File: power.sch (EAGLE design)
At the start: 27 parts

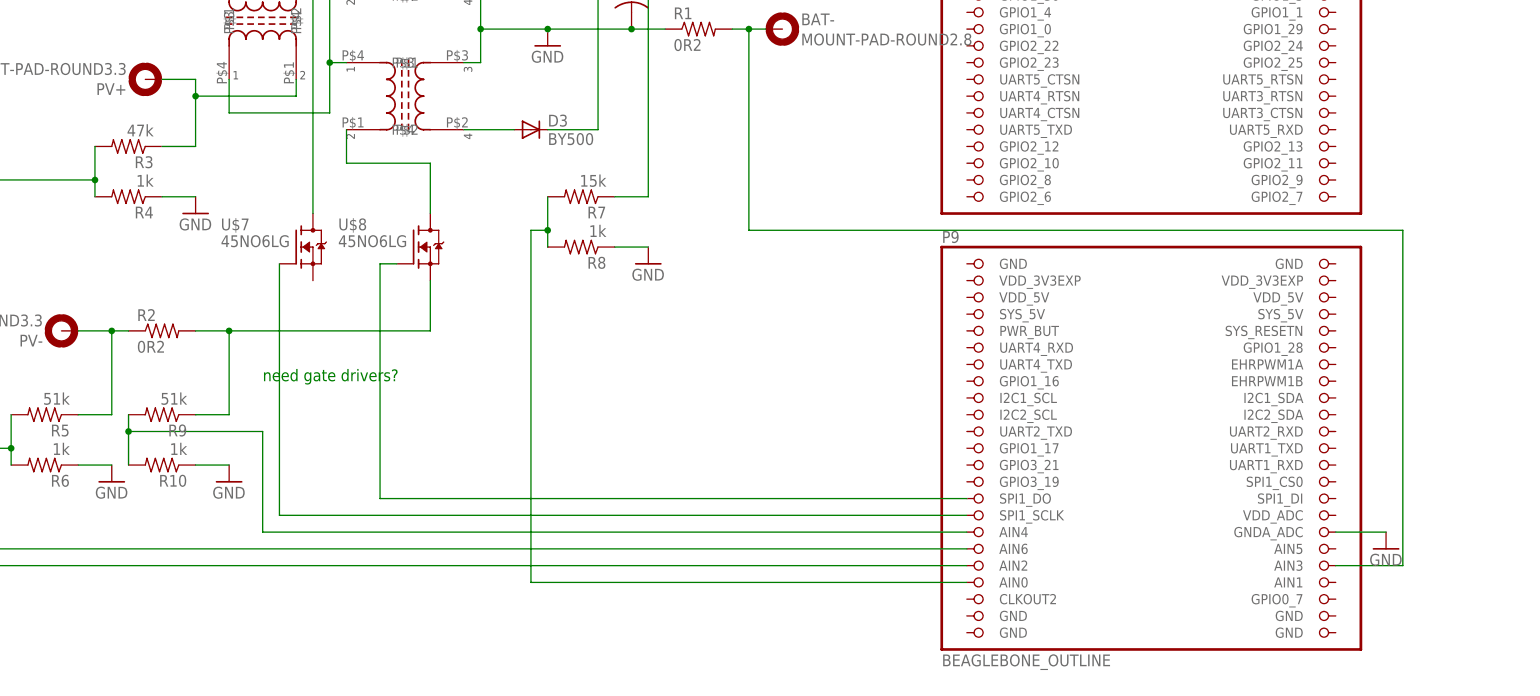
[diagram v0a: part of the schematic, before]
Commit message: more board and schematic fixes.  added slightly negative voltage reference hack.
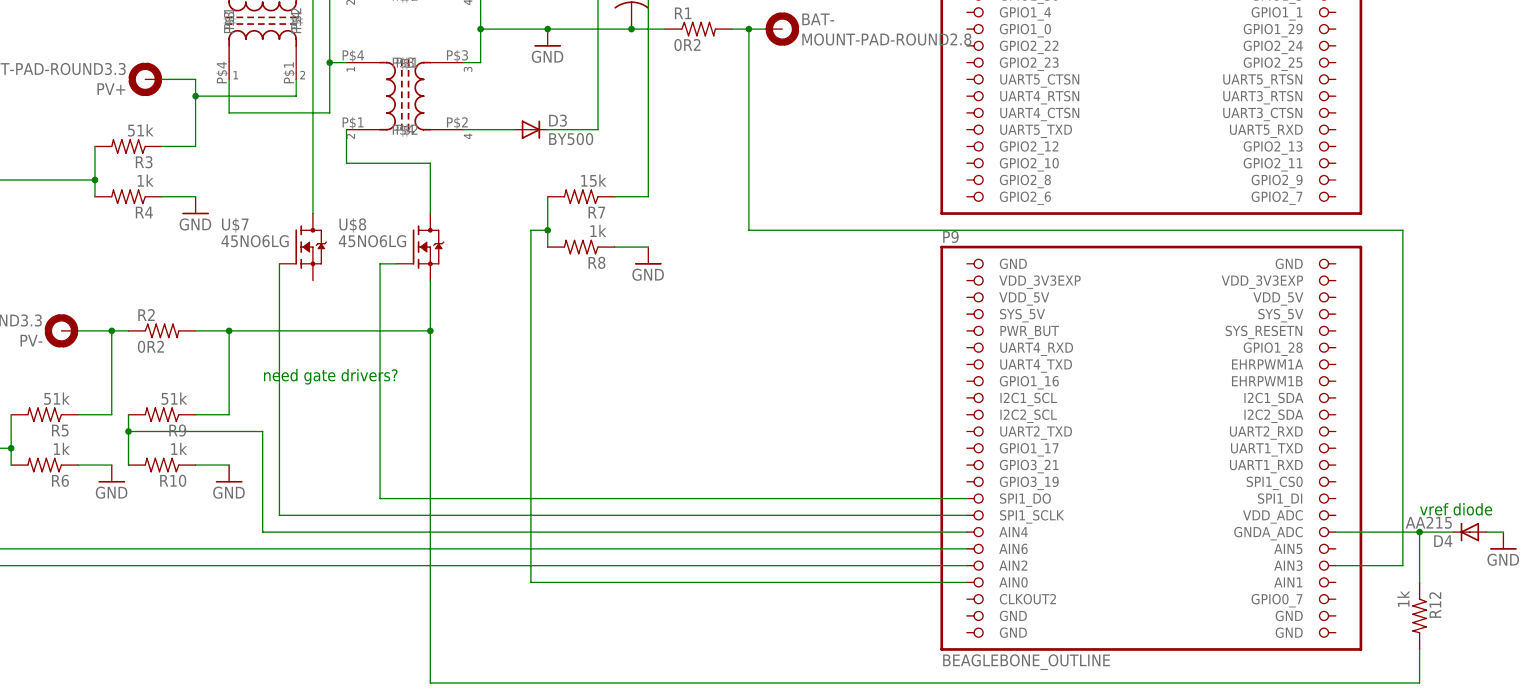
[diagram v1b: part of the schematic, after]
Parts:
- added D4: AA215, diode:AA215
- added R12: 1k, rcl:R-US_R0603
- R3: value 47k -> 51k
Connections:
- new net N$14: D4.C, R12.1, U$6.GNDA_ADC
- net GND: now also D4.A; no longer U$6.GNDA_ADC
- net N$8: now also R12.2
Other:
- note added: "vref diode"
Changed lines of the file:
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@@
 <part name="U$6" library="adafruit" deviceset="BEAGLEBONE_OUTLINE" device=""/>
 <part name="GND1" library="supply1" deviceset="GND" device=""/>
-<part name="R3" library="rcl" deviceset="R-US_" device="R0603" value="47k"/>
+<part name="R3" library="rcl" deviceset="R-US_" device="R0603" value="51k"/>
 <part name="R4" library="rcl" deviceset="R-US_" device="R0603" value="1k"/>
 <part name="GND2" library="supply1" deviceset="GND" device=""/>
@@
 <part name="H3" library="holes" deviceset="MOUNT-PAD-ROUND" device="2.8"/>
 <part name="R7" library="rcl" deviceset="R-US_" device="R0603" value="15k"/>
+<part name="D4" library="diode" deviceset="AA215" device=""/>
+<part name="R12" library="rcl" deviceset="R-US_" device="R0603" value="1k"/>
 <part name="GND7" library="supply1" deviceset="GND" device=""/>
 </parts>
@@
 <plain>
 <text x="17.78" y="-2.54" size="1.778" layer="91">need gate drivers?</text>
+<text x="193.04" y="-22.86" size="1.778" layer="91">vref diode</text>
 </plain>
 <instances>
@@
 <instance part="H3" gate="G$1" x="83.82" y="81.28"/>
 <instance part="R7" gate="G$1" x="66.04" y="25.4" rot="R180"/>
-<instance part="GND7" gate="1" x="187.96" y="-27.94"/>
+<instance part="D4" gate="1" x="200.66" y="-25.4" rot="R180"/>
+<instance part="R12" gate="G$1" x="193.04" y="-38.1" rot="R270"/>
+<instance part="GND7" gate="1" x="205.74" y="-27.94"/>
 </instances>
 <busses>
@@
 </segment>
 <segment>
-<pinref part="GND7" gate="1" pin="GND"/>
-<pinref part="U$6" gate="G$1" pin="GNDA_ADC"/>
-<wire x1="180.34" y1="-25.4" x2="187.96" y2="-25.4" width="0.1524" layer="91"/>
-</segment>
-<segment>
 <pinref part="R8" gate="G$1" pin="1"/>
 <wire x1="71.12" y1="17.78" x2="76.2" y2="17.78" width="0.1524" layer="91"/>
@@
 <wire x1="78.74" y1="81.28" x2="78.74" y2="76.2" width="0.1524" layer="91"/>
 <junction x="78.74" y="76.2"/>
+</segment>
+<segment>
+<pinref part="GND7" gate="1" pin="GND"/>
+<pinref part="D4" gate="1" pin="A"/>
+<wire x1="205.74" y1="-25.4" x2="203.2" y2="-25.4" width="0.1524" layer="91"/>
 </segment>
 </net>
@@
 <pinref part="U$8" gate="G$1" pin="S"/>
 <wire x1="43.18" y1="12.7" x2="43.18" y2="5.08" width="0.1524" layer="91"/>
+<wire x1="43.18" y1="5.08" x2="43.18" y2="-48.26" width="0.1524" layer="91"/>
+<wire x1="43.18" y1="-48.26" x2="193.04" y2="-48.26" width="0.1524" layer="91"/>
+<junction x="43.18" y="5.08"/>
+<pinref part="R12" gate="G$1" pin="2"/>
+<wire x1="193.04" y1="-43.18" x2="193.04" y2="-48.26" width="0.1524" layer="91"/>
 </segment>
 </net>
@@
 </segment>
 </net>
+<net name="N$14" class="0">
+<segment>
+<pinref part="U$6" gate="G$1" pin="GNDA_ADC"/>
+<wire x1="180.34" y1="-25.4" x2="193.04" y2="-25.4" width="0.1524" layer="91"/>
+<pinref part="D4" gate="1" pin="C"/>
+<pinref part="R12" gate="G$1" pin="1"/>
+<wire x1="193.04" y1="-25.4" x2="198.12" y2="-25.4" width="0.1524" layer="91"/>
+<wire x1="193.04" y1="-33.02" x2="193.04" y2="-25.4" width="0.1524" layer="91"/>
+<junction x="193.04" y="-25.4"/>
+</segment>
+</net>

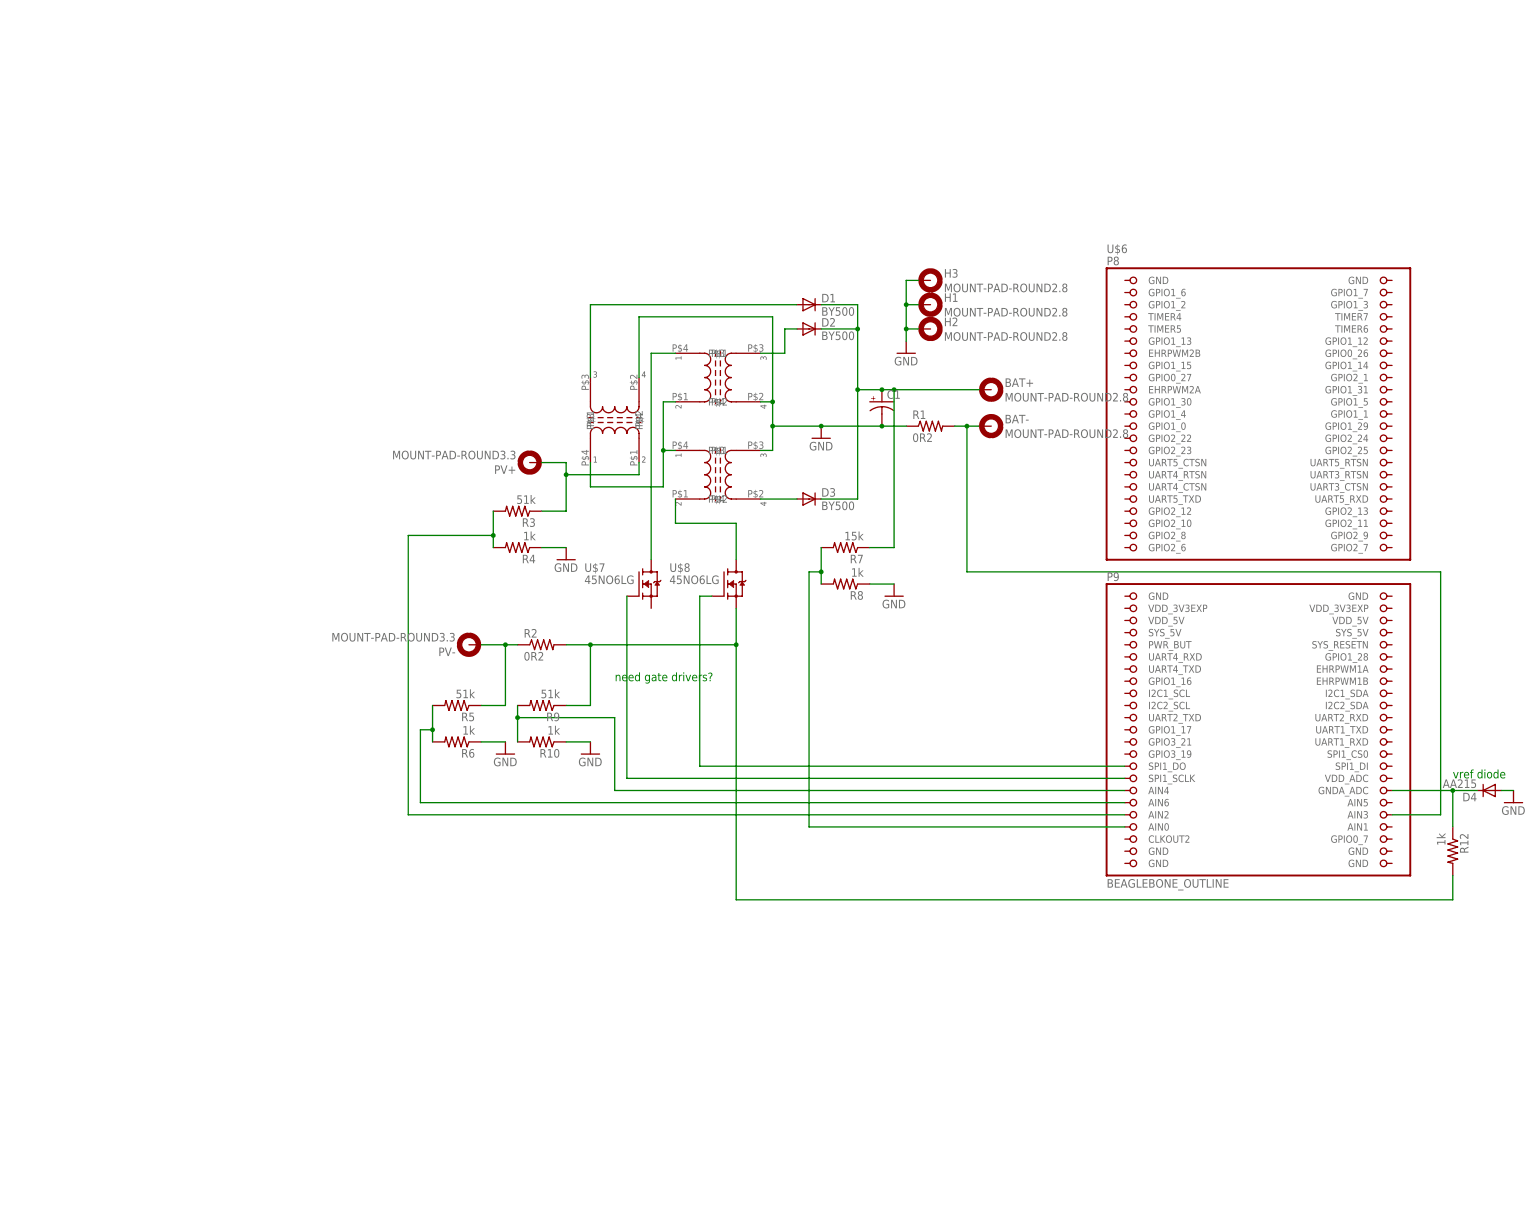
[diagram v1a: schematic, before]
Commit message: made things more complicated, fixed a schematic mistake, added gate drivers
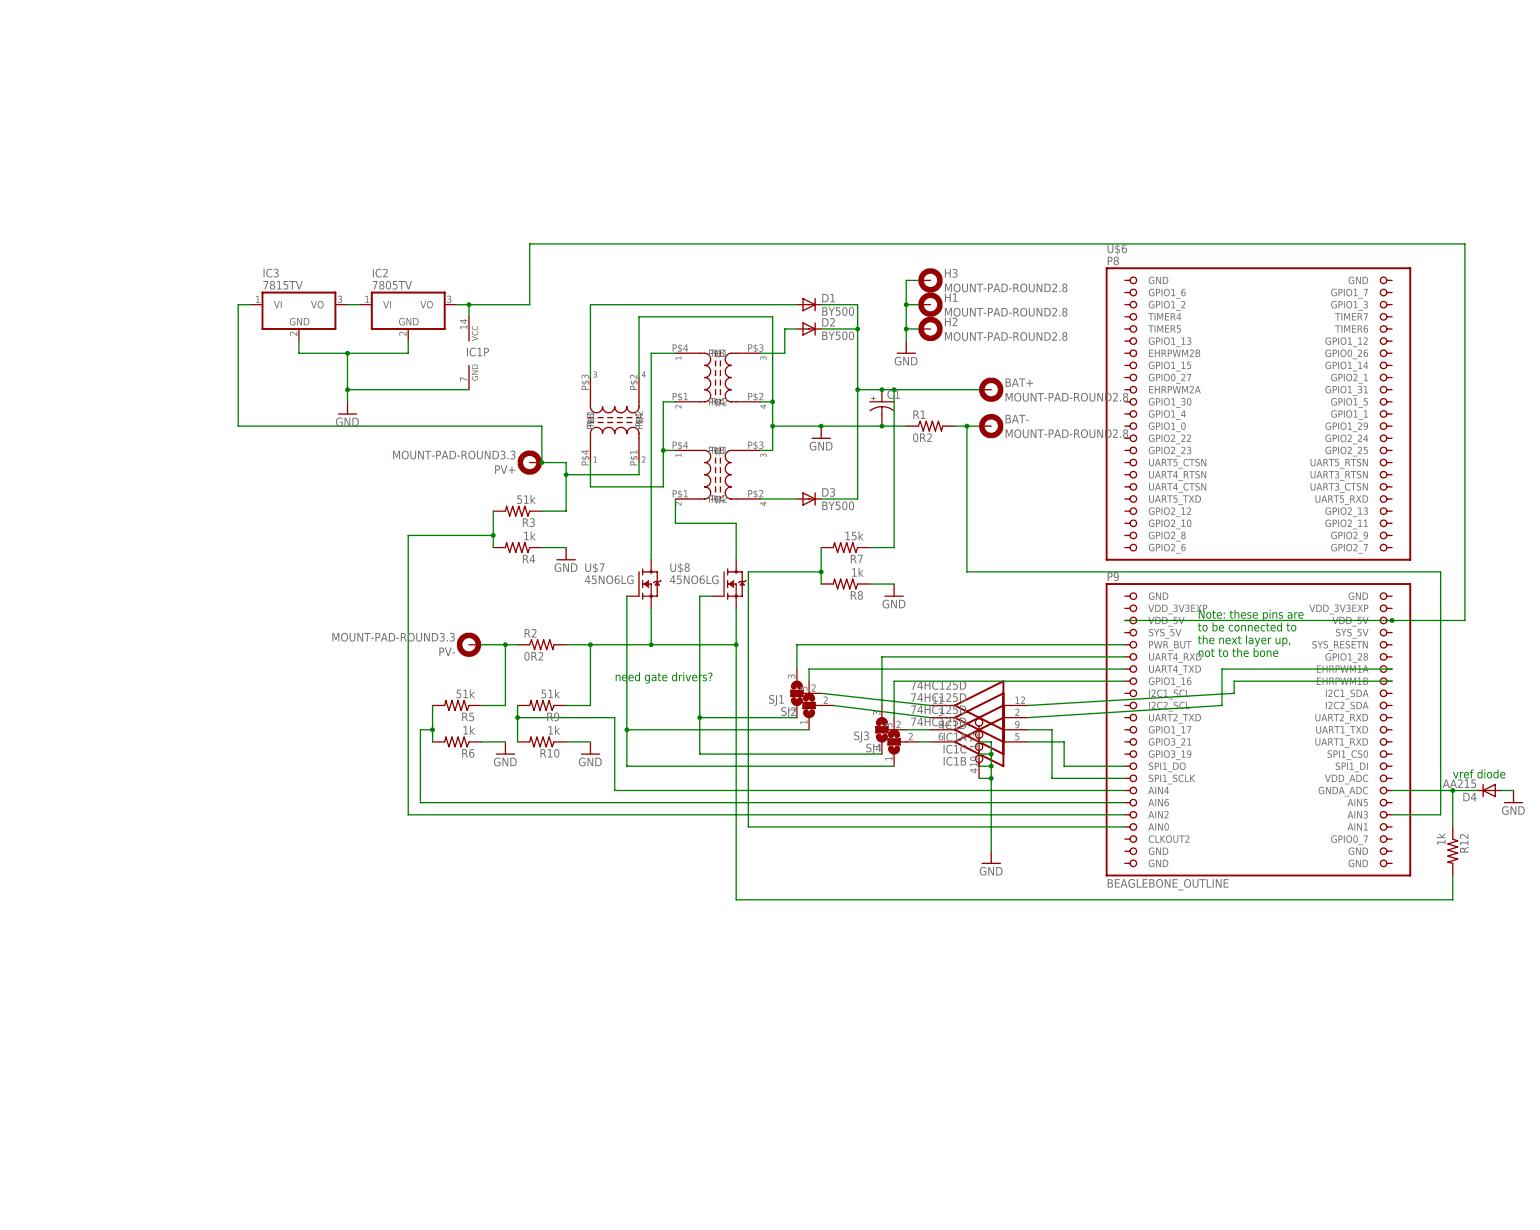
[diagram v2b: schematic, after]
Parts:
- added IC1: 74HC125D, 74xx-eu:74HC125D
- added IC2: 7805TV, linear:7805TV
- added IC3: 7815TV, linear:7815TV
- added SJ1, SJ2, SJ3, SJ4: (no value), jumper:SJ2W
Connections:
- new net N$23: IC1A.I, U$6.EHRPWM1A
- new net N$26: IC1P.VCC, IC2.VO, U$6.VDD_5V@1, U$6.VDD_5V@2
- new net N$27: IC2.VI, IC3.VO
- new net N$28: IC1D.I, U$6.EHRPWM1B
- new net N$29: IC1C.O, SJ3.2
- new net N$30: IC1B.O, SJ4.2
- new net N$31: SJ4.3, U$6.GPIO1_16
- new net N$32: SJ3.3, U$6.UART4_RXD
- new net N$33: SJ2.3, U$6.UART4_TXD
- new net N$34: SJ1.3, U$6.PWR_BUT
- new net N$35: IC1D.O, SJ1.2
- new net N$36: IC1A.O, SJ2.2
- new net N$37: IC1B.I, U$6.SPI1_DO
- new net N$38: IC1C.I, U$6.SPI1_SCLK
- net GND: now also IC1A.OE, IC1B.OE, IC1C.OE, IC1D.OE, IC1P.GND, IC2.GND, IC3.GND
- net N$11: now also SJ1.1, SJ3.1; no longer U$6.SPI1_DO
- net N$13: now also SJ2.1, SJ4.1; no longer U$6.SPI1_SCLK
- net N$3: now also IC3.VI
- net N$8: now also U$7.S
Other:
- note added: "Note: these pins are to be connected to the next layer up, not to the bone"

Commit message: fixed more things, probably broke more things in the process
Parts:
- U$6: device adafruit:BEAGLEBONE_OUTLINE -> bone:BEAGLEBONE_OUTLINE
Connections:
- net N$23: now also U$6.GPIO3_19, U$6.SPI1_CS0
- net N$28: now also U$6.GPIO3_21, U$6.UART1_RXD
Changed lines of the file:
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@@
 <part name="U$4" library="chokes" deviceset="TLF14CBH3321R0K1" device=""/>
 <part name="U$5" library="chokes" deviceset="TLF14CBH3321R0K1" device=""/>
-<part name="U$6" library="adafruit" deviceset="BEAGLEBONE_OUTLINE" device=""/>
+<part name="U$6" library="bone" deviceset="BEAGLEBONE_OUTLINE" device=""/>
 <part name="GND1" library="supply1" deviceset="GND" device=""/>
 <part name="R3" library="rcl" deviceset="R-US_" device="R0603" value="51k"/>
@@
 <text x="17.78" y="-2.54" size="1.778" layer="91">need gate drivers?</text>
 <text x="193.04" y="-22.86" size="1.778" layer="91">vref diode</text>
-<text x="139.7" y="2.54" size="1.778" layer="91">Note: these pins are
+<text x="139.7" y="-22.86" size="1.778" layer="91">Note: these pins are
 to be connected to
 the next layer up,
@@
 <pinref part="IC1" gate="A" pin="I"/>
 <wire x1="144.78" y1="-7.62" x2="104.14" y2="-10.16" width="0.1524" layer="91"/>
+<pinref part="U$6" gate="G$1" pin="GPIO3_19"/>
+<wire x1="124.46" y1="-17.78" x2="144.78" y2="-17.78" width="0.1524" layer="91"/>
+<wire x1="144.78" y1="-17.78" x2="144.78" y2="-7.62" width="0.1524" layer="91"/>
+<junction x="144.78" y="-7.62"/>
+<pinref part="U$6" gate="G$1" pin="SPI1_CS0"/>
+<wire x1="144.78" y1="-17.78" x2="180.34" y2="-17.78" width="0.1524" layer="91"/>
+<junction x="144.78" y="-17.78"/>
 </segment>
 </net>
@@
 <pinref part="IC1" gate="D" pin="I"/>
 <wire x1="104.14" y1="-7.62" x2="147.32" y2="-5.08" width="0.1524" layer="91"/>
-</segment>
-</net>
+<pinref part="U$6" gate="G$1" pin="GPIO3_21"/>
+<wire x1="124.46" y1="-15.24" x2="147.32" y2="-15.24" width="0.1524" layer="91"/>
+<wire x1="147.32" y1="-15.24" x2="147.32" y2="-5.08" width="0.1524" layer="91"/>
+<junction x="147.32" y="-5.08"/>
+<pinref part="U$6" gate="G$1" pin="UART1_RXD"/>
+<wire x1="180.34" y1="-15.24" x2="147.32" y2="-15.24" width="0.1524" layer="91"/>
+<junction x="147.32" y="-15.24"/>
+</segment>
+</net>
